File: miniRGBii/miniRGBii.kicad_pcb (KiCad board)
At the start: 2 copper layers, 29.2 x 43.2 mm, 25 parts

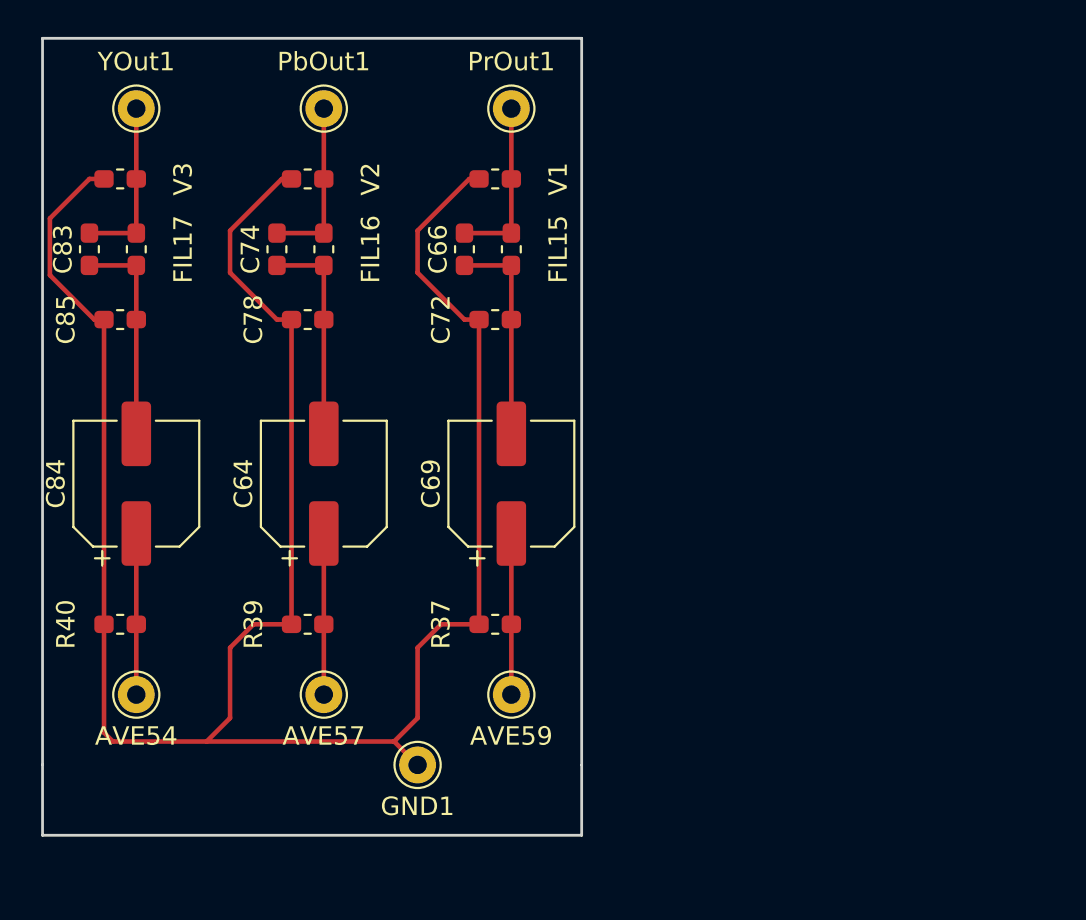
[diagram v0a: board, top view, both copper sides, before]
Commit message: Renamed project, trimmed pcb design
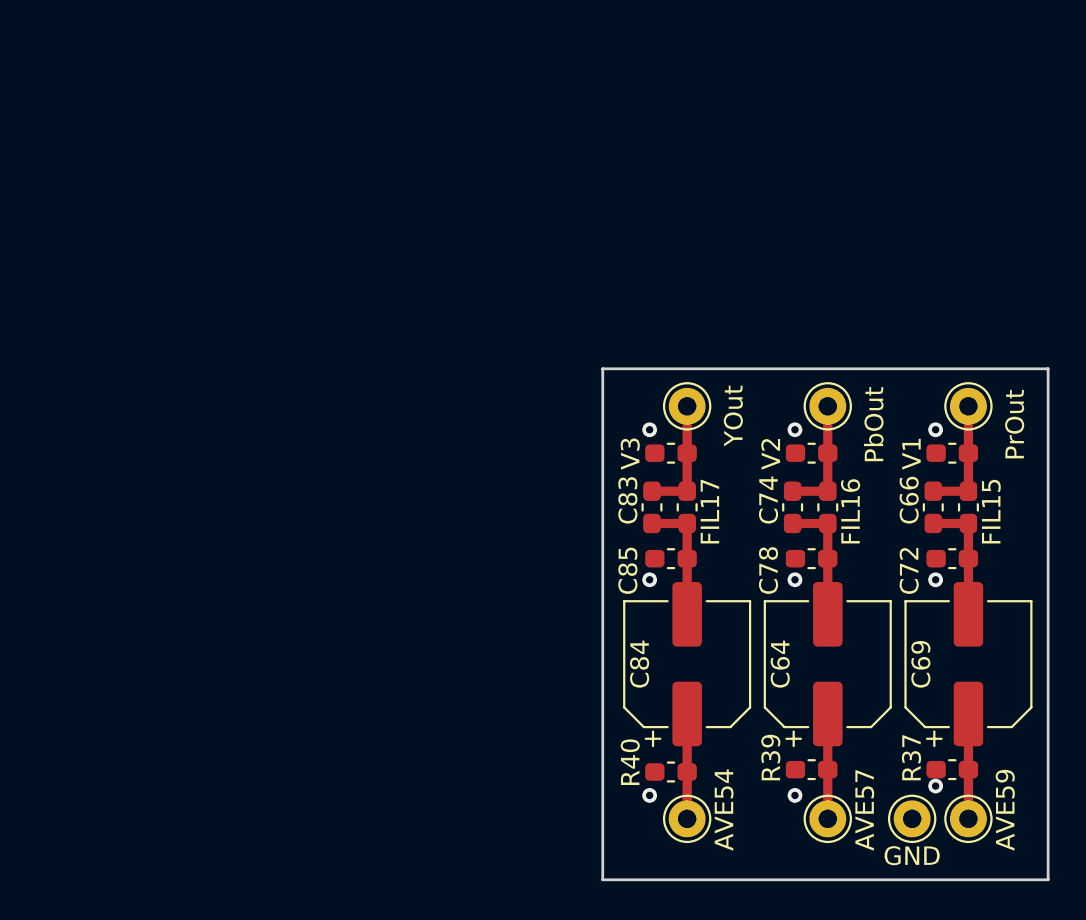
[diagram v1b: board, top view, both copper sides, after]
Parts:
- removed PbOut1: TestPoint, Connector_Pin:Pin_D1.0mm_L10.0mm
- added PbOut: TestPoint, Connector_Pin:Pin_D1.0mm_L10.0mm, F.Cu at (140.3, 91.1)
- moved YOut 33.9 mm to (132.7, 91.1)
- moved C83 33.5 mm to (130.8, 96.5)
- moved V3 33.3 mm to (131.8, 93.6)
- moved FIL17 33.0 mm to (132.7, 96.5)
- moved C85 32.5 mm to (131.8, 99.3)
- moved C84 31.4 mm to (132.7, 105.0)
- moved C74 31.2 mm to (138.4, 96.5)
- moved V2 31.1 mm to (139.5, 93.6)
- moved R40 30.9 mm to (131.8, 110.9)
- moved FIL16 30.7 mm to (140.3, 96.5)
- moved AVE54 30.6 mm to (132.7, 113.4)
- moved C78 30.2 mm to (139.5, 99.3)
- moved PrOut 29.6 mm to (148.0, 91.1)
- moved C64 29.0 mm to (140.3, 105.0)
- moved C66 29.0 mm to (146.1, 96.5)
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- renumbered GND1 to GND, PrOut1 to PrOut, YOut1 to YOut
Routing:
- net GND: track 125.2 -> 0.00 mm, vias 0 -> 9
- net Net-(C83-Pad1): track 11.7 -> 6.82 mm
- net Net-(C64-Pad2): track 11.7 -> 6.82 mm
- net Net-(C66-Pad1): track 11.7 -> 6.82 mm
- net Net-(AVE59-Pad1): track 8.73 -> 5.68 mm
- net Net-(AVE57-Pad1): track 8.73 -> 5.68 mm
- net Net-(C83-Pad2): track 9.28 -> 6.51 mm
- net Net-(C74-Pad2): track 9.28 -> 6.51 mm
- net Net-(C66-Pad2): track 9.28 -> 6.51 mm
- net Net-(AVE54-Pad1): track 8.73 -> 6.19 mm
- added copper zone on B.Cu, net GND
- added copper zone on F.Cu, net GND
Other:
- board size 29.2 x 43.2 mm -> 24.1 x 27.7 mm
- net class GND added: clearance 0.4, trace_width 0.5, via_dia 0.8, via_drill 0.4
- board text added: "Consolebytes.com"
- board text added: "Did you wire your ground?"
- board text added: "Don’t forget this BLAHHH!"
- board text added: "by Commandblock6417"
- board text added: "miniRGBii Rev. 1.0"

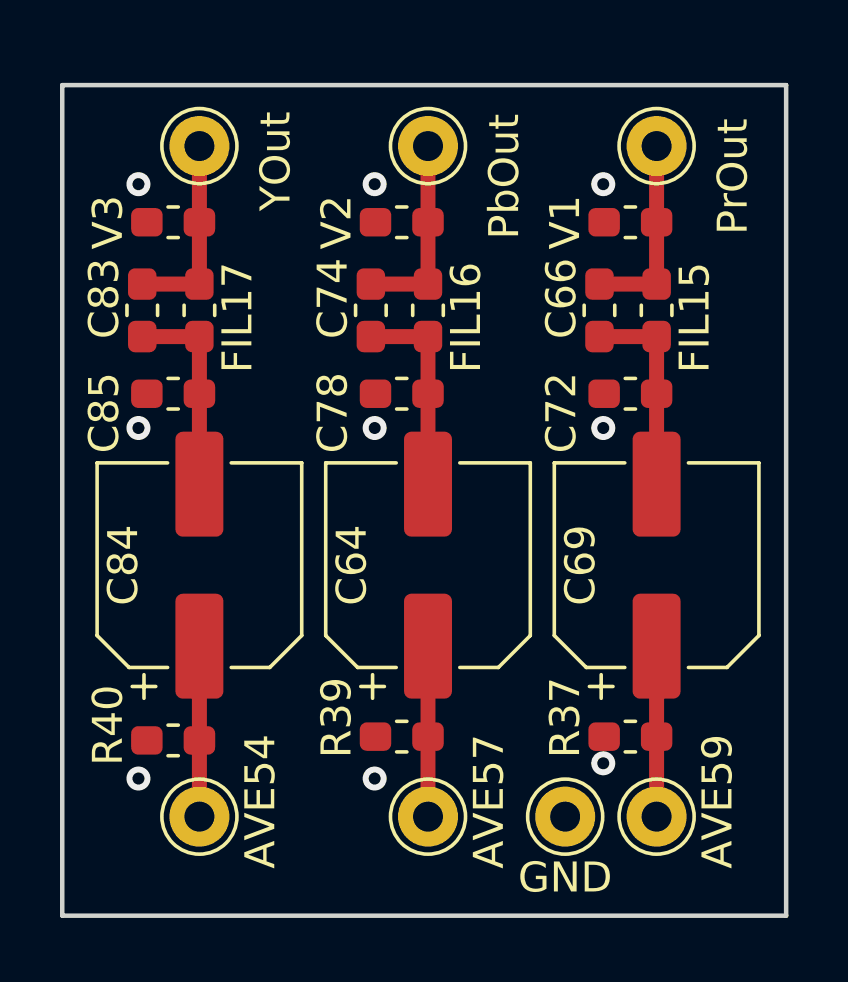
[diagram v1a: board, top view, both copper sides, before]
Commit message: Changed the board to utilise lower profile capacitors
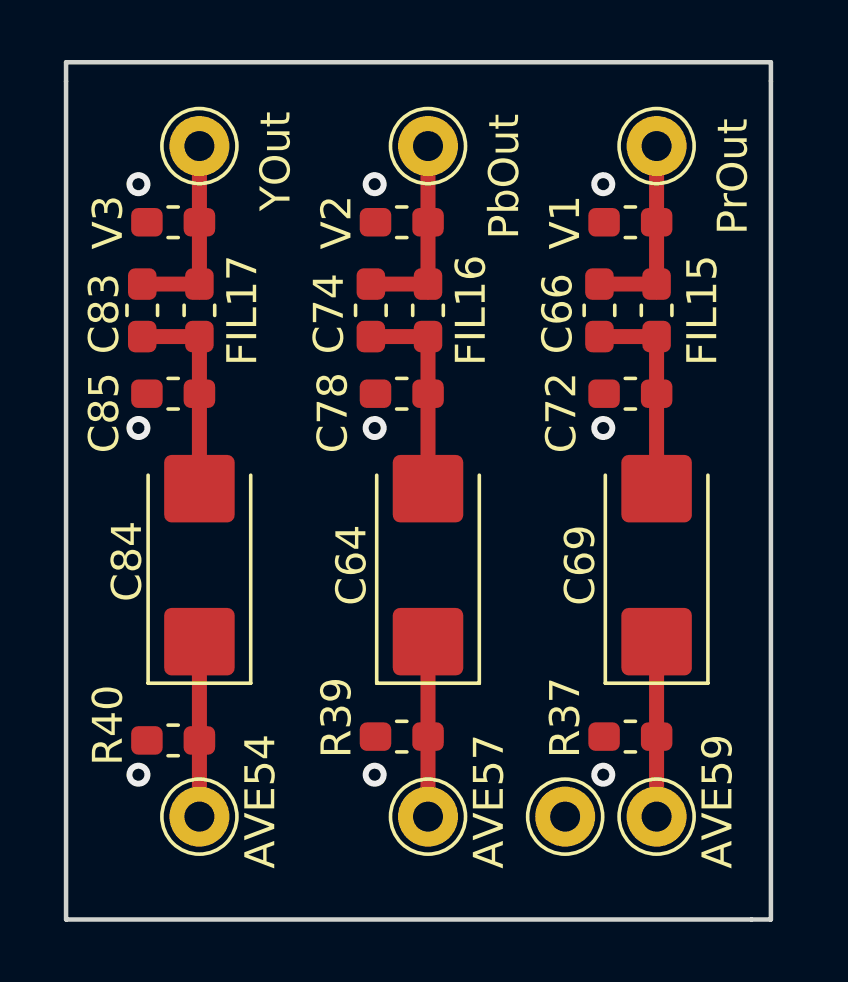
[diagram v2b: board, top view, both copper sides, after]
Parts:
- C64, C69, C84: footprint Capacitor_SMD:CP_Elec_6.3x3 -> Capacitor_Tantalum_SMD:CP_EIA-6032-28_Kemet-C_Pad2.25x2.35mm_HandSolder
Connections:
- net Net-(AVE54-Pad1) renamed AVE54
- net Net-(AVE57-Pad1) renamed AVE57
- net Net-(AVE59-Pad1) renamed AVE59
- net Net-(C66-Pad2) renamed PrOut
- net Net-(C74-Pad2) renamed PbOut
- net Net-(C83-Pad2) renamed YOut
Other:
- board size 24.1 x 27.7 mm -> 23.5 x 28.6 mm
- board text added: "miniRGBii Rev. 1.1"
- board text removed: "Consolebytes.com"
- board text removed: "miniRGBii Rev. 1.0"
